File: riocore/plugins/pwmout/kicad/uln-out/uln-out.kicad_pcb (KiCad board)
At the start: 2 copper layers, 23 x 35.2 mm, 17 parts, among them J1 691305130006, U11 ULN2803A

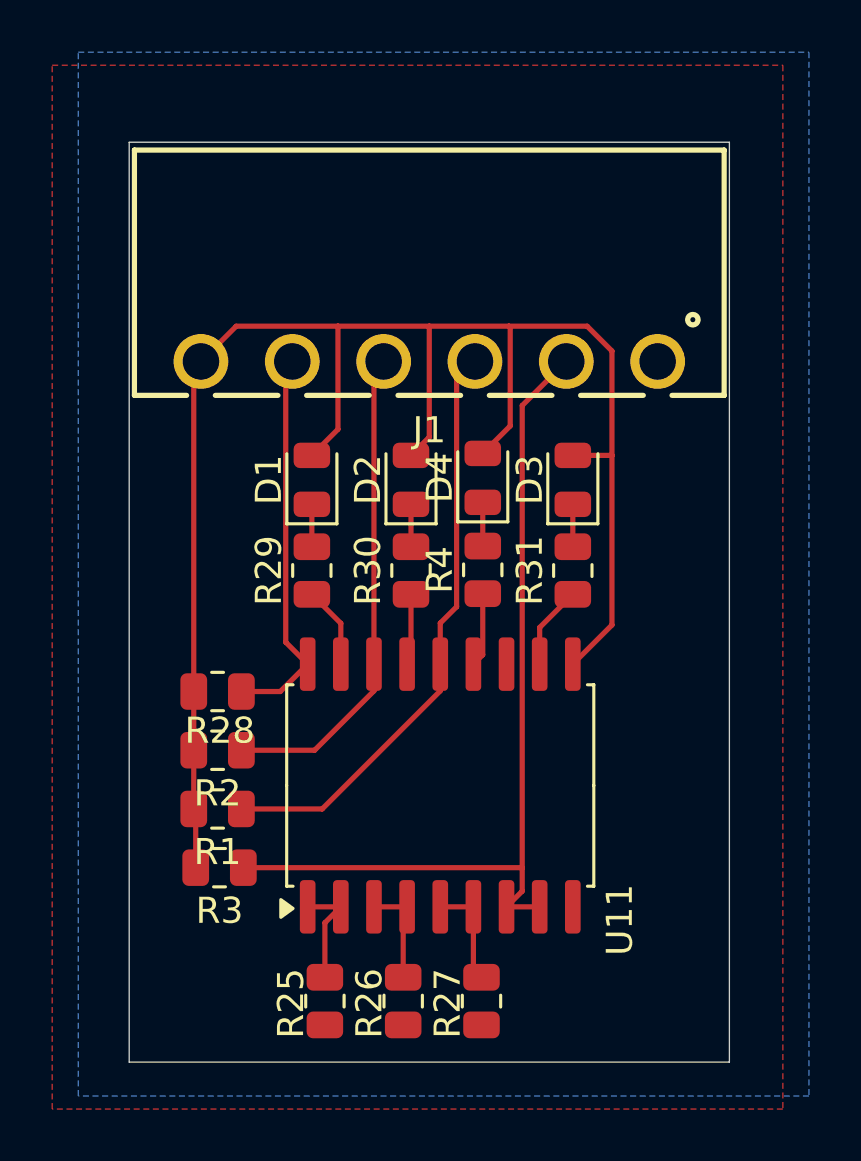
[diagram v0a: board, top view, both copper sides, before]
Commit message: kicad: pin positions
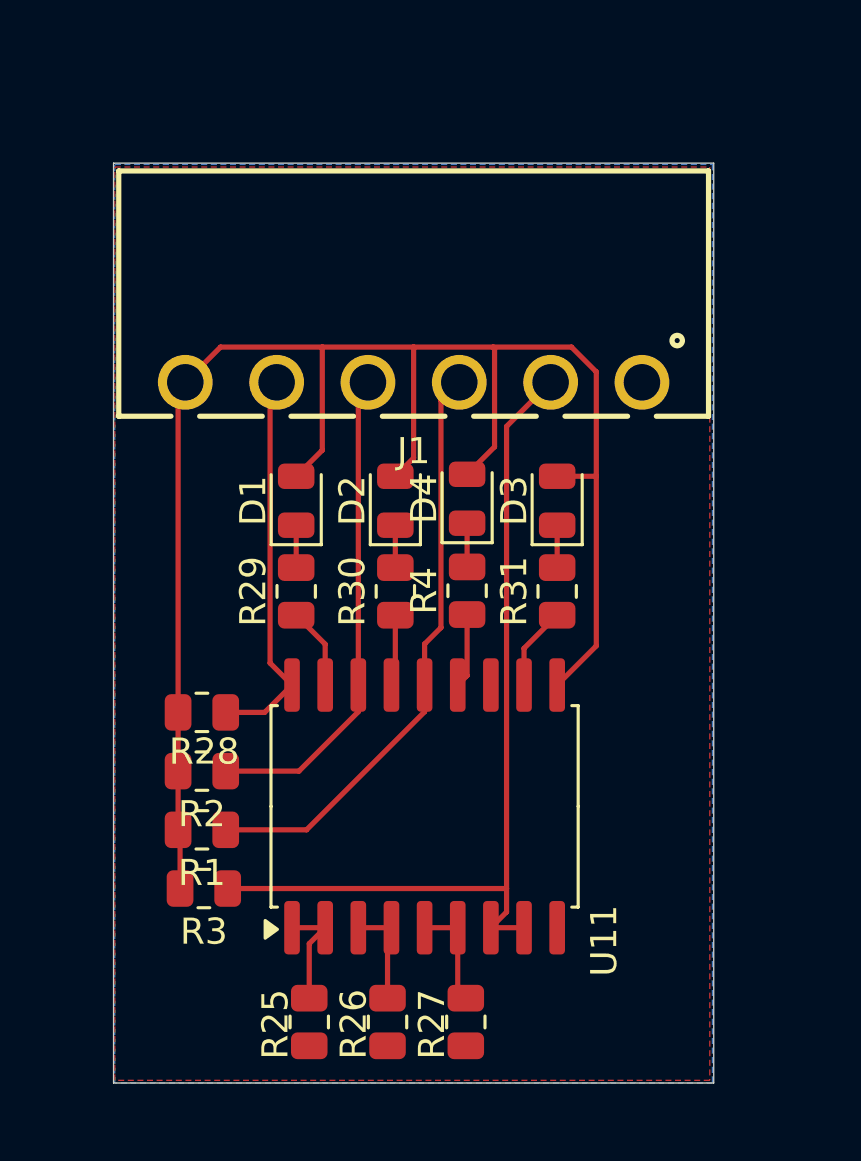
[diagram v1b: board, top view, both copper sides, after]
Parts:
- J1: value 691305130006 -> pwmout
- moved U11 1.00 mm to (140.8, 98.9)
- moved D1 1.00 mm to (135.9, 87.2)
- moved D2 1.00 mm to (139.7, 87.2)
- moved D3 1.00 mm to (145.9, 87.2)
- moved D4 1.00 mm to (142.4, 87.1)
- moved J1 1.00 mm to (140.4, 82.7)
- moved R1 1.00 mm to (132.2, 99.8)
- moved R2 1.00 mm to (132.2, 97.5)
- moved R25 1.00 mm to (136.4, 107.2)
- moved R26 1.00 mm to (139.4, 107.2)
- moved R27 1.00 mm to (142.4, 107.2)
- moved R28 1.00 mm to (132.2, 95.3)
- moved R29 1.00 mm to (135.9, 90.7)
- moved R3 1.00 mm to (132.3, 102.0)
- moved R30 1.00 mm to (139.7, 90.7)
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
